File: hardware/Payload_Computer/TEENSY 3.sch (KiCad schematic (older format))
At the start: 9 parts

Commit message: More Library Updates
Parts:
- U?: symbol Payload_Computer-rescue:MK20DX256VLH7-Symbols -> Symbols:MK20DX256VLH7
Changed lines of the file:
@@
 	2150 3150 2450 3150
 $Comp
-L Payload_Computer-rescue:MK20DX256VLH7-Symbols U?
+L Symbols:MK20DX256VLH7 U?
 U 1 1 5FAEECCE
 P 3550 3850

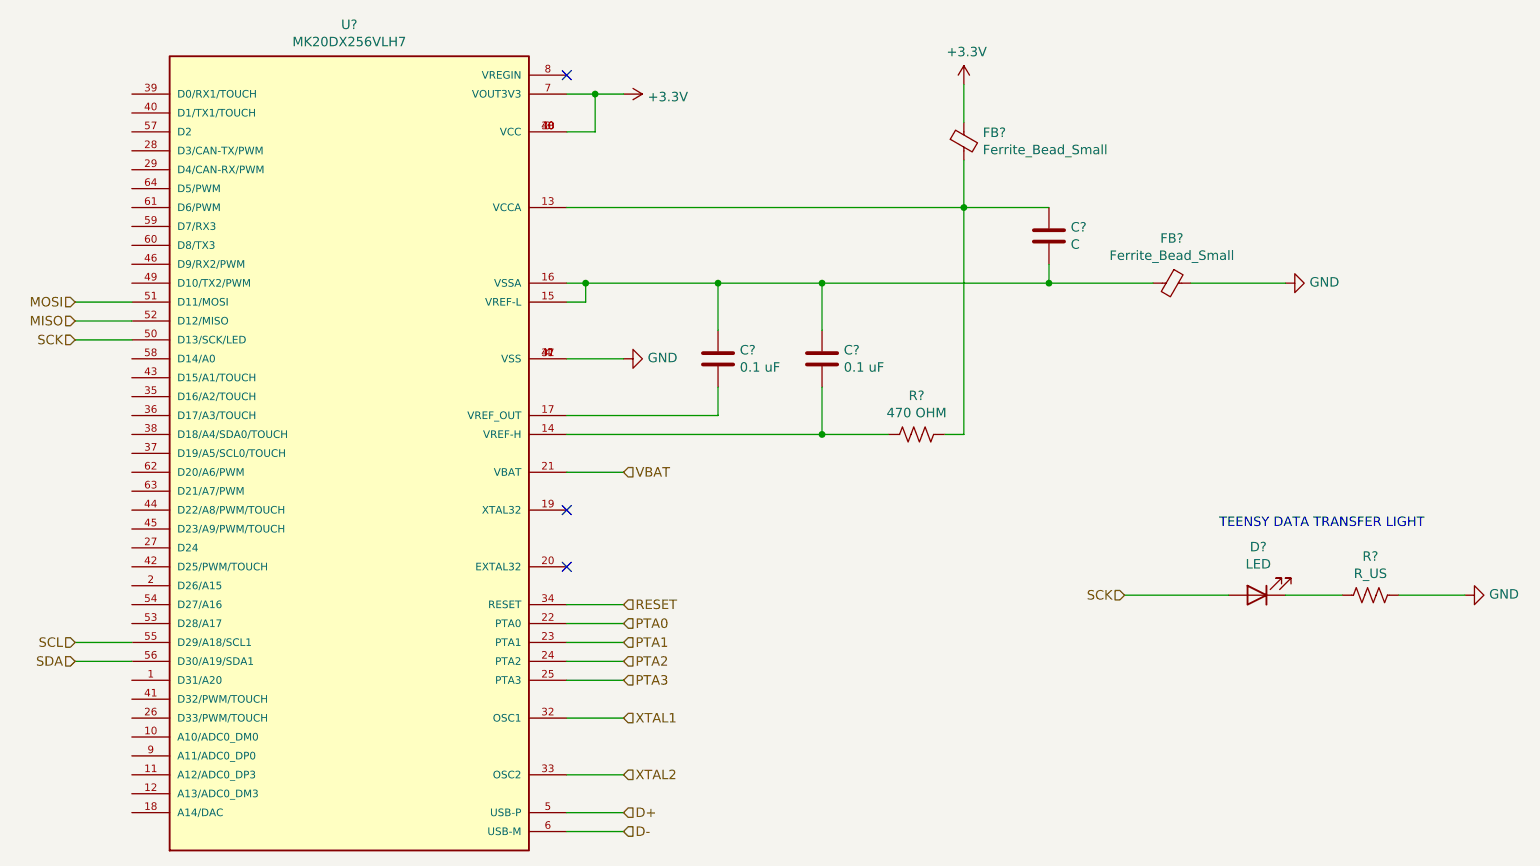
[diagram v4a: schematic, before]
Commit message: Finished Fan Schematic. Working on Servos
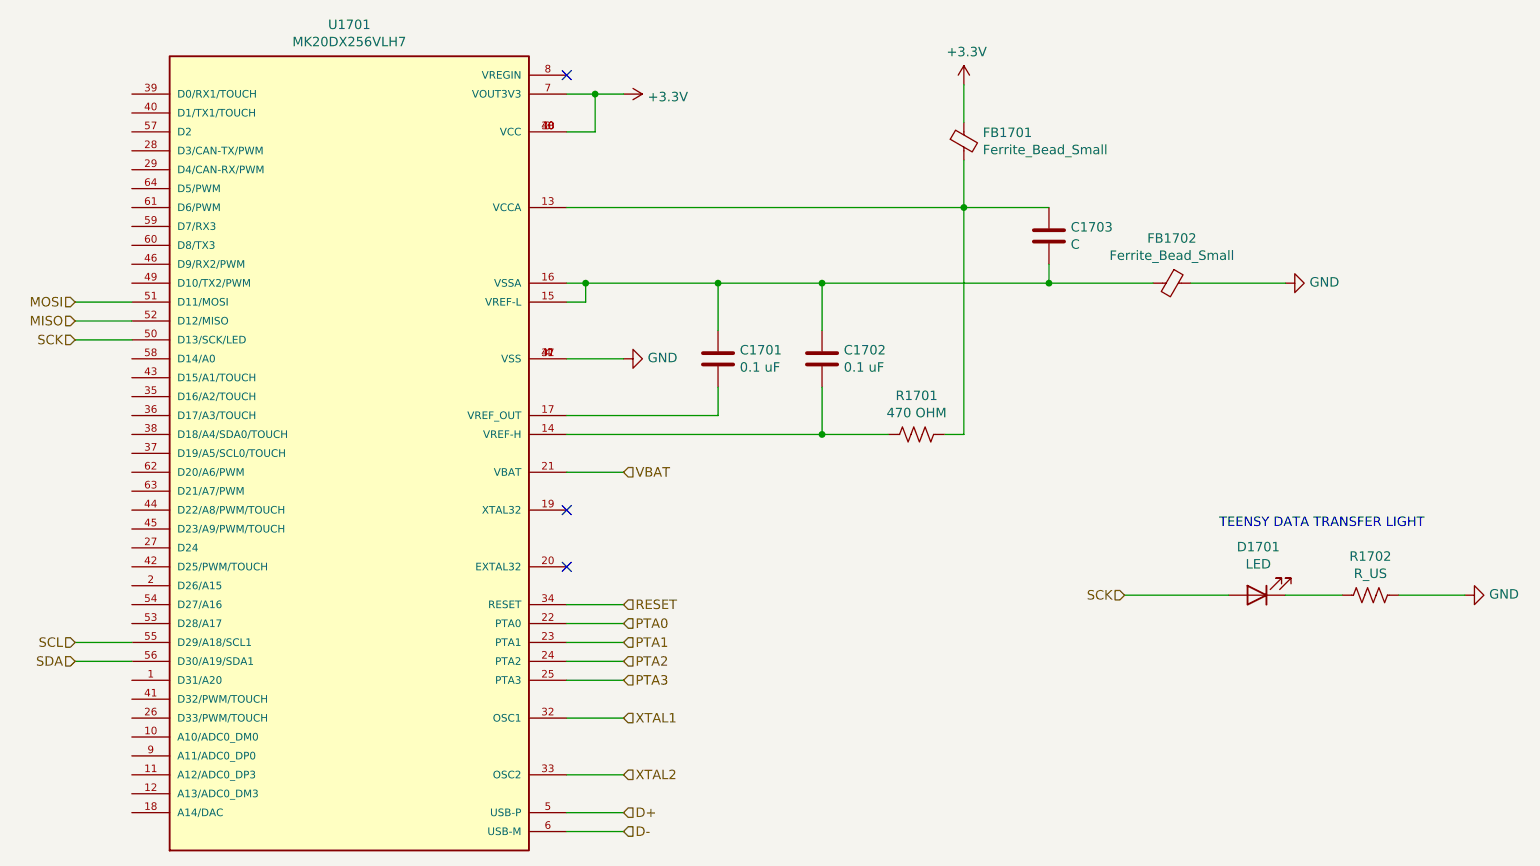
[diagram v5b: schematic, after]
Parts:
- C901, C902, C903: renamed from C?; footprint (none) -> Capacitor_SMD:C_0603_1608Metric_Pad1.08x0.95mm_HandSolder
- R901, R902: renamed from R?; footprint (none) -> Resistor_SMD:R_0603_1608Metric_Pad0.98x0.95mm_HandSolder
- gave numbers to parts that had none: 4
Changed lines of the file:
@@
 $Descr A4 11693 8268
 encoding utf-8
-Sheet 13 26
+Sheet 17 22
 Title ""
 Date ""
@@
 	2150 3150 2450 3150
 $Comp
-L Symbols:MK20DX256VLH7 U?
+L Symbols:MK20DX256VLH7 U901
 U 1 1 5FAEECCE
 P 3550 3850
-AR Path="/5F84585C/5FAEECCE" Ref="U?"  Part="1"
-AR Path="/6028538E/5FAEECCE" Ref="U?"  Part="1"
-F 0 "U?" H 3600 6217 50  0000 C CNN
+AR Path="/5F84585C/5FAEECCE" Ref="U901"  Part="1"
+AR Path="/6028538E/5FAEECCE" Ref="U1701"  Part="1"
+F 0 "U1701" H 3600 6217 50  0000 C CNN
 F 1 "MK20DX256VLH7" H 3600 6126 50  0000 C CNN
 F 2 "QFP50P1200X1200X160-64N" H 3550 3850 50  0001 L BNN
@@
 	5050 5750 4750 5750
 $Comp
-L power:GND #PWR?
+L power:GND #PWR0902
 U 1 1 5FAF5AFB
 P 5050 3250
-AR Path="/5F84585C/5FAF5AFB" Ref="#PWR?"  Part="1"
-AR Path="/6028538E/5FAF5AFB" Ref="#PWR?"  Part="1"
-F 0 "#PWR?" H 5050 3000 50  0001 C CNN
+AR Path="/5F84585C/5FAF5AFB" Ref="#PWR0902"  Part="1"
+AR Path="/6028538E/5FAF5AFB" Ref="#PWR01702"  Part="1"
+F 0 "#PWR01702" H 5050 3000 50  0001 C CNN
 F 1 "GND" V 5055 3122 50  0000 R CNN
 F 2 "" H 5050 3250 50  0001 C CNN
@@
 NoConn ~ 4750 1750
 $Comp
-L power:+3.3V #PWR?
+L power:+3.3V #PWR0901
 U 1 1 5FB25063
 P 5050 1850
-AR Path="/5F84585C/5FB25063" Ref="#PWR?"  Part="1"
-AR Path="/6028538E/5FB25063" Ref="#PWR?"  Part="1"
-F 0 "#PWR?" H 5050 1700 50  0001 C CNN
+AR Path="/5F84585C/5FB25063" Ref="#PWR0901"  Part="1"
+AR Path="/6028538E/5FB25063" Ref="#PWR01701"  Part="1"
+F 0 "#PWR01701" H 5050 1700 50  0001 C CNN
 F 1 "+3.3V" V 5065 1978 50  0000 L CNN
 F 2 "" H 5050 1850 50  0001 C CNN
@@
 	4900 1850 5050 1850
 $Comp
-L Device:Ferrite_Bead_Small FB?
+L Device:Ferrite_Bead_Small FB902
 U 1 1 5FB25D65
 P 7950 2850
-AR Path="/5F84585C/5FB25D65" Ref="FB?"  Part="1"
-AR Path="/6028538E/5FB25D65" Ref="FB?"  Part="1"
-F 0 "FB?" V 7713 2850 50  0000 C CNN
+AR Path="/5F84585C/5FB25D65" Ref="FB902"  Part="1"
+AR Path="/6028538E/5FB25D65" Ref="FB1702"  Part="1"
+F 0 "FB1702" V 7713 2850 50  0000 C CNN
 F 1 "Ferrite_Bead_Small" V 7804 2850 50  0000 C CNN
 F 2 "" V 7880 2850 50  0001 C CNN
@@
 $EndComp
 $Comp
-L Device:Ferrite_Bead_Small FB?
+L Device:Ferrite_Bead_Small FB901
 U 1 1 5FB25F1D
 P 6850 2100
-AR Path="/5F84585C/5FB25F1D" Ref="FB?"  Part="1"
-AR Path="/6028538E/5FB25F1D" Ref="FB?"  Part="1"
-F 0 "FB?" H 6950 2146 50  0000 L CNN
+AR Path="/5F84585C/5FB25F1D" Ref="FB901"  Part="1"
+AR Path="/6028538E/5FB25F1D" Ref="FB1701"  Part="1"
+F 0 "FB1701" H 6950 2146 50  0000 L CNN
 F 1 "Ferrite_Bead_Small" H 6950 2055 50  0000 L CNN
 F 2 "" V 6780 2100 50  0001 C CNN
@@
 $EndComp
 $Comp
-L Device:C C?
+L Device:C C901
 U 1 1 5FB264DD
 P 5550 3250
-AR Path="/5F84585C/5FB264DD" Ref="C?"  Part="1"
-AR Path="/6028538E/5FB264DD" Ref="C?"  Part="1"
-F 0 "C?" H 5665 3296 50  0000 L CNN
+AR Path="/5F84585C/5FB264DD" Ref="C901"  Part="1"
+AR Path="/6028538E/5FB264DD" Ref="C1701"  Part="1"
+F 0 "C1701" H 5665 3296 50  0000 L CNN
 F 1 "0.1 uF" H 5665 3205 50  0000 L CNN
-F 2 "" H 5588 3100 50  0001 C CNN
+F 2 "Capacitor_SMD:C_0603_1608Metric_Pad1.08x0.95mm_HandSolder" H 5588 3100 50  0001 C CNN
 F 3 "~" H 5550 3250 50  0001 C CNN
 	1    5550 3250
@@
 $EndComp
 $Comp
-L Device:C C?
+L Device:C C902
 U 1 1 5FB269BF
 P 6100 3250
-AR Path="/5F84585C/5FB269BF" Ref="C?"  Part="1"
-AR Path="/6028538E/5FB269BF" Ref="C?"  Part="1"
-F 0 "C?" H 6215 3296 50  0000 L CNN
+AR Path="/5F84585C/5FB269BF" Ref="C902"  Part="1"
+AR Path="/6028538E/5FB269BF" Ref="C1702"  Part="1"
+F 0 "C1702" H 6215 3296 50  0000 L CNN
 F 1 "0.1 uF" H 6215 3205 50  0000 L CNN
-F 2 "" H 6138 3100 50  0001 C CNN
+F 2 "Capacitor_SMD:C_0603_1608Metric_Pad1.08x0.95mm_HandSolder" H 6138 3100 50  0001 C CNN
 F 3 "~" H 6100 3250 50  0001 C CNN
 	1    6100 3250
@@
 $EndComp
 $Comp
-L Device:C C?
+L Device:C C903
 U 1 1 5FB26BB3
 P 7300 2600
-AR Path="/5F84585C/5FB26BB3" Ref="C?"  Part="1"
-AR Path="/6028538E/5FB26BB3" Ref="C?"  Part="1"
-F 0 "C?" H 7415 2646 50  0000 L CNN
+AR Path="/5F84585C/5FB26BB3" Ref="C903"  Part="1"
+AR Path="/6028538E/5FB26BB3" Ref="C1703"  Part="1"
+F 0 "C1703" H 7415 2646 50  0000 L CNN
 F 1 "C" H 7415 2555 50  0000 L CNN
-F 2 "" H 7338 2450 50  0001 C CNN
+F 2 "Capacitor_SMD:C_0603_1608Metric_Pad1.08x0.95mm_HandSolder" H 7338 2450 50  0001 C CNN
 F 3 "~" H 7300 2600 50  0001 C CNN
 	1    7300 2600
@@
 $EndComp
 $Comp
-L Device:R_US R?
+L Device:R_US R901
 U 1 1 5FB270F2
 P 6600 3650
-AR Path="/5F84585C/5FB270F2" Ref="R?"  Part="1"
-AR Path="/6028538E/5FB270F2" Ref="R?"  Part="1"
-F 0 "R?" V 6395 3650 50  0000 C CNN
+AR Path="/5F84585C/5FB270F2" Ref="R901"  Part="1"
+AR Path="/6028538E/5FB270F2" Ref="R1701"  Part="1"
+F 0 "R1701" V 6395 3650 50  0000 C CNN
 F 1 "470 OHM" V 6486 3650 50  0000 C CNN
-F 2 "" V 6640 3640 50  0001 C CNN
+F 2 "Resistor_SMD:R_0603_1608Metric_Pad0.98x0.95mm_HandSolder" V 6640 3640 50  0001 C CNN
 F 3 "~" H 6600 3650 50  0001 C CNN
 	1    6600 3650
@@
 Connection ~ 7300 2850
 $Comp
-L power:GND #PWR?
+L power:GND #PWR0904
 U 1 1 5FB34D78
 P 8550 2850
-AR Path="/5F84585C/5FB34D78" Ref="#PWR?"  Part="1"
-AR Path="/6028538E/5FB34D78" Ref="#PWR?"  Part="1"
-F 0 "#PWR?" H 8550 2600 50  0001 C CNN
+AR Path="/5F84585C/5FB34D78" Ref="#PWR0904"  Part="1"
+AR Path="/6028538E/5FB34D78" Ref="#PWR01704"  Part="1"
+F 0 "#PWR01704" H 8550 2600 50  0001 C CNN
 F 1 "GND" V 8555 2722 50  0000 R CNN
 F 2 "" H 8550 2850 50  0001 C CNN
@@
 	6850 2200 6850 2450
 $Comp
-L power:+3.3V #PWR?
+L power:+3.3V #PWR0903
 U 1 1 5FB376D9
 P 6850 1800
-AR Path="/5F84585C/5FB376D9" Ref="#PWR?"  Part="1"
-AR Path="/6028538E/5FB376D9" Ref="#PWR?"  Part="1"
-F 0 "#PWR?" H 6850 1650 50  0001 C CNN
+AR Path="/5F84585C/5FB376D9" Ref="#PWR0903"  Part="1"
+AR Path="/6028538E/5FB376D9" Ref="#PWR01703"  Part="1"
+F 0 "#PWR01703" H 6850 1650 50  0001 C CNN
 F 1 "+3.3V" H 6865 1973 50  0000 C CNN
 F 2 "" H 6850 1800 50  0001 C CNN
@@
 	2450 4850 2150 4850
 $Comp
-L Device:LED D?
+L Device:LED D901
 U 1 1 5FC23755
 P 8400 4500
-AR Path="/5F84585C/5FC23755" Ref="D?"  Part="1"
-AR Path="/6028538E/5FC23755" Ref="D?"  Part="1"
-F 0 "D?" H 8393 4245 50  0000 C CNN
+AR Path="/5F84585C/5FC23755" Ref="D901"  Part="1"
+AR Path="/6028538E/5FC23755" Ref="D1701"  Part="1"
+F 0 "D1701" H 8393 4245 50  0000 C CNN
 F 1 "LED" H 8393 4336 50  0000 C CNN
 F 2 "" H 8400 4500 50  0001 C CNN
@@
 $EndComp
 $Comp
-L Device:R_US R?
+L Device:R_US R902
 U 1 1 5FC24323
 P 9000 4500
-AR Path="/5F84585C/5FC24323" Ref="R?"  Part="1"
-AR Path="/6028538E/5FC24323" Ref="R?"  Part="1"
-F 0 "R?" V 8795 4500 50  0000 C CNN
+AR Path="/5F84585C/5FC24323" Ref="R902"  Part="1"
+AR Path="/6028538E/5FC24323" Ref="R1702"  Part="1"
+F 0 "R1702" V 8795 4500 50  0000 C CNN
 F 1 "R_US" V 8886 4500 50  0000 C CNN
-F 2 "" V 9040 4490 50  0001 C CNN
+F 2 "Resistor_SMD:R_0603_1608Metric_Pad0.98x0.95mm_HandSolder" V 9040 4490 50  0001 C CNN
 F 3 "~" H 9000 4500 50  0001 C CNN
 	1    9000 4500
@@
 	7700 4500 8250 4500
 $Comp
-L power:GND #PWR?
+L power:GND #PWR0905
 U 1 1 5FC264A5
 P 9500 4500
-AR Path="/5F84585C/5FC264A5" Ref="#PWR?"  Part="1"
-AR Path="/6028538E/5FC264A5" Ref="#PWR?"  Part="1"
-F 0 "#PWR?" H 9500 4250 50  0001 C CNN
+AR Path="/5F84585C/5FC264A5" Ref="#PWR0905"  Part="1"
+AR Path="/6028538E/5FC264A5" Ref="#PWR01705"  Part="1"
+F 0 "#PWR01705" H 9500 4250 50  0001 C CNN
 F 1 "GND" V 9505 4372 50  0000 R CNN
 F 2 "" H 9500 4500 50  0001 C CNN

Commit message: Minor Changes
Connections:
- net VBAT is gone; now on net +3V3: U901.21 (VBAT)
- net D25: now reaches U901.42 (D25/PWM/TOUCH)
- net PWM3: now reaches U901.44 (D22/A8/PWM/TOUCH)
- net PWM4: now reaches U901.45 (D23/A9/PWM/TOUCH)
- net PWM1: now reaches U901.62 (D20/A6/PWM)
- net PWM2: now reaches U901.63 (D21/A7/PWM)
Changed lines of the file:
@@
 $Descr A4 11693 8268
 encoding utf-8
-Sheet 17 22
+Sheet 18 18
 Title ""
 Date ""
@@
 Text Notes 8200 4150 0    50   ~ 0
 TEENSY DATA TRANSFER LIGHT\n
-Text HLabel 5050 3850 2    50   Input ~ 0
-VBAT
 Wire Wire Line
 	5050 3850 4750 3850
+$Comp
+L power:+3.3V #PWR01806
+U 1 1 602FCEF8
+P 5050 3850
+AR Path="/6028538E/602FCEF8" Ref="#PWR01806"  Part="1"
+AR Path="/5F84585C/602FCEF8" Ref="#PWR01706"  Part="1"
+F 0 "#PWR01806" H 5050 3700 50  0001 C CNN
+F 1 "+3.3V" V 5065 3978 50  0000 L CNN
+F 2 "" H 5050 3850 50  0001 C CNN
+F 3 "" H 5050 3850 50  0001 C CNN
+	1    5050 3850
+	0    1    1    0
+$EndComp
+Text HLabel 2150 3850 0    50   Input ~ 0
+PWM1
+Text HLabel 2150 3950 0    50   Input ~ 0
+PWM2
+Text HLabel 2150 4050 0    50   Input ~ 0
+PWM3
+Text HLabel 2150 4150 0    50   Input ~ 0
+PWM4
+Wire Wire Line
+	2150 3850 2450 3850
+Wire Wire Line
+	2150 3950 2450 3950
+Wire Wire Line
+	2150 4050 2450 4050
+Wire Wire Line
+	2150 4150 2450 4150
+Text HLabel 2150 4350 0    50   Input ~ 0
+D25
+Wire Wire Line
+	2150 4350 2450 4350
 $EndSCHEMATC

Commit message: Added some footprints
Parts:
- FB901, FB902: footprint (none) -> Capacitor_SMD:C_0603_1608Metric_Pad1.08x0.95mm_HandSolder
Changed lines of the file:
@@
 F 0 "FB1702" V 7713 2850 50  0000 C CNN
 F 1 "Ferrite_Bead_Small" V 7804 2850 50  0000 C CNN
-F 2 "" V 7880 2850 50  0001 C CNN
+F 2 "Capacitor_SMD:C_0603_1608Metric_Pad1.08x0.95mm_HandSolder" V 7880 2850 50  0001 C CNN
 F 3 "~" H 7950 2850 50  0001 C CNN
 	1    7950 2850
@@
 F 0 "FB1701" H 6950 2146 50  0000 L CNN
 F 1 "Ferrite_Bead_Small" H 6950 2055 50  0000 L CNN
-F 2 "" V 6780 2100 50  0001 C CNN
+F 2 "Capacitor_SMD:C_0603_1608Metric_Pad1.08x0.95mm_HandSolder" V 6780 2100 50  0001 C CNN
 F 3 "~" H 6850 2100 50  0001 C CNN
 	1    6850 2100

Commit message: Added footprints to fuse and led
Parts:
- D901: footprint (none) -> LED_SMD:LED_0603_1608Metric_Pad1.05x0.95mm_HandSolder
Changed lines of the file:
@@
 F 0 "D1701" H 8393 4245 50  0000 C CNN
 F 1 "LED" H 8393 4336 50  0000 C CNN
-F 2 "" H 8400 4500 50  0001 C CNN
+F 2 "LED_SMD:LED_0603_1608Metric_Pad1.05x0.95mm_HandSolder" H 8400 4500 50  0001 C CNN
 F 3 "~" H 8400 4500 50  0001 C CNN
 	1    8400 4500
